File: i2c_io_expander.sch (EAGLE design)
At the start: 21 parts, among them IC1 MCP23017SP, J1 43814-6621, J6 22-23-2031

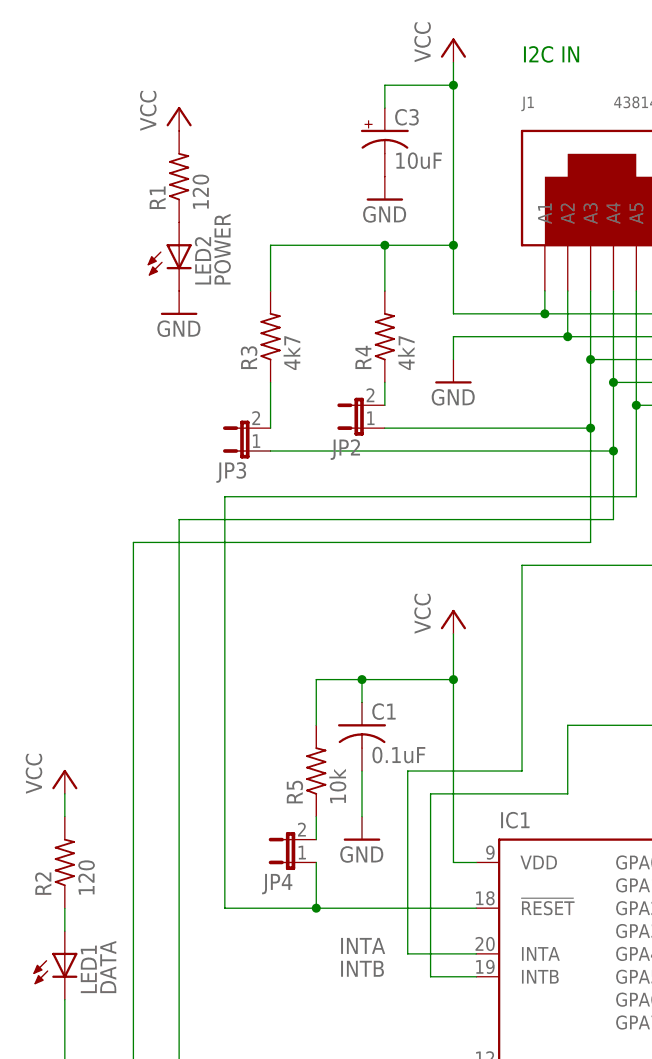
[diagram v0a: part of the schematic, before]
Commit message: Added contact info and rev # to silkscreen Added VCC and GND designator to silkscreen
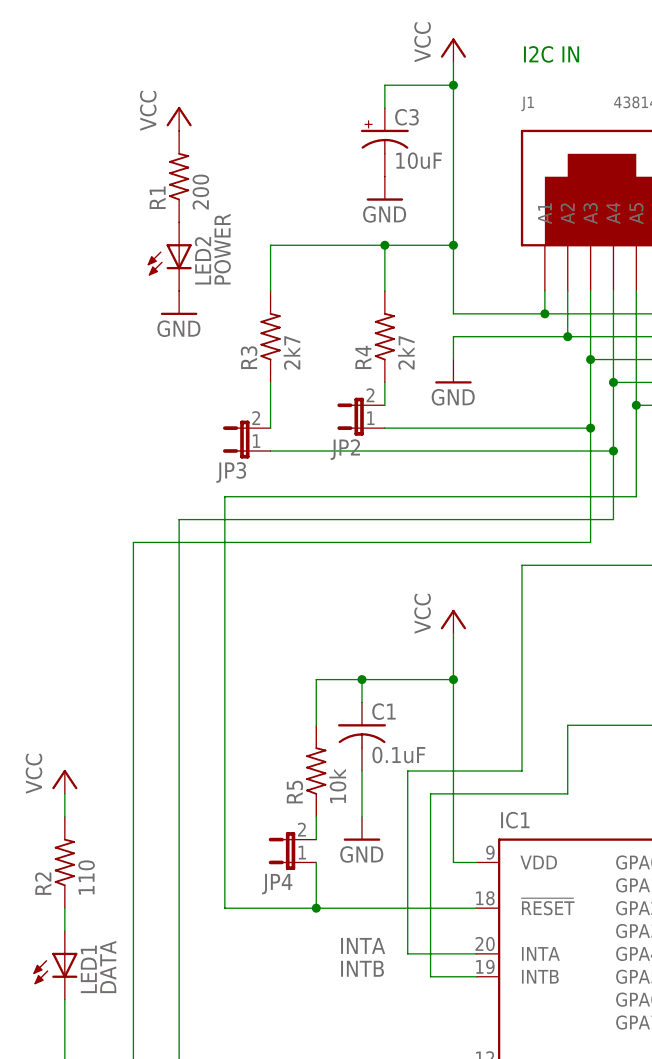
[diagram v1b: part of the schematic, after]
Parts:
- R1: value 120 -> 200
- R2: value 120 -> 110
- R3, R4: value 4k7 -> 2k7
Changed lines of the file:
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@@
 <attribute name="OC_NEWARK" value="unknown"/>
 </part>
-<part name="R1" library="rcl" deviceset="R-US_" device="R0603" value="120">
+<part name="R1" library="rcl" deviceset="R-US_" device="R0603" value="200">
 <attribute name="MF" value=""/>
 <attribute name="MPN" value=""/>
 <attribute name="OC_NEWARK" value="unknown"/>
 </part>
-<part name="R2" library="rcl" deviceset="R-US_" device="R0603" value="120">
+<part name="R2" library="rcl" deviceset="R-US_" device="R0603" value="110">
 <attribute name="MF" value=""/>
 <attribute name="MPN" value=""/>
 <attribute name="OC_NEWARK" value="unknown"/>
 </part>
-<part name="R3" library="rcl" deviceset="R-US_" device="R0603" value="4k7">
+<part name="R3" library="rcl" deviceset="R-US_" device="R0603" value="2k7">
 <attribute name="MF" value=""/>
 <attribute name="MPN" value=""/>
 <attribute name="OC_NEWARK" value="unknown"/>
 </part>
-<part name="R4" library="rcl" deviceset="R-US_" device="R0603" value="4k7">
+<part name="R4" library="rcl" deviceset="R-US_" device="R0603" value="2k7">
 <attribute name="MF" value=""/>
 <attribute name="MPN" value=""/>

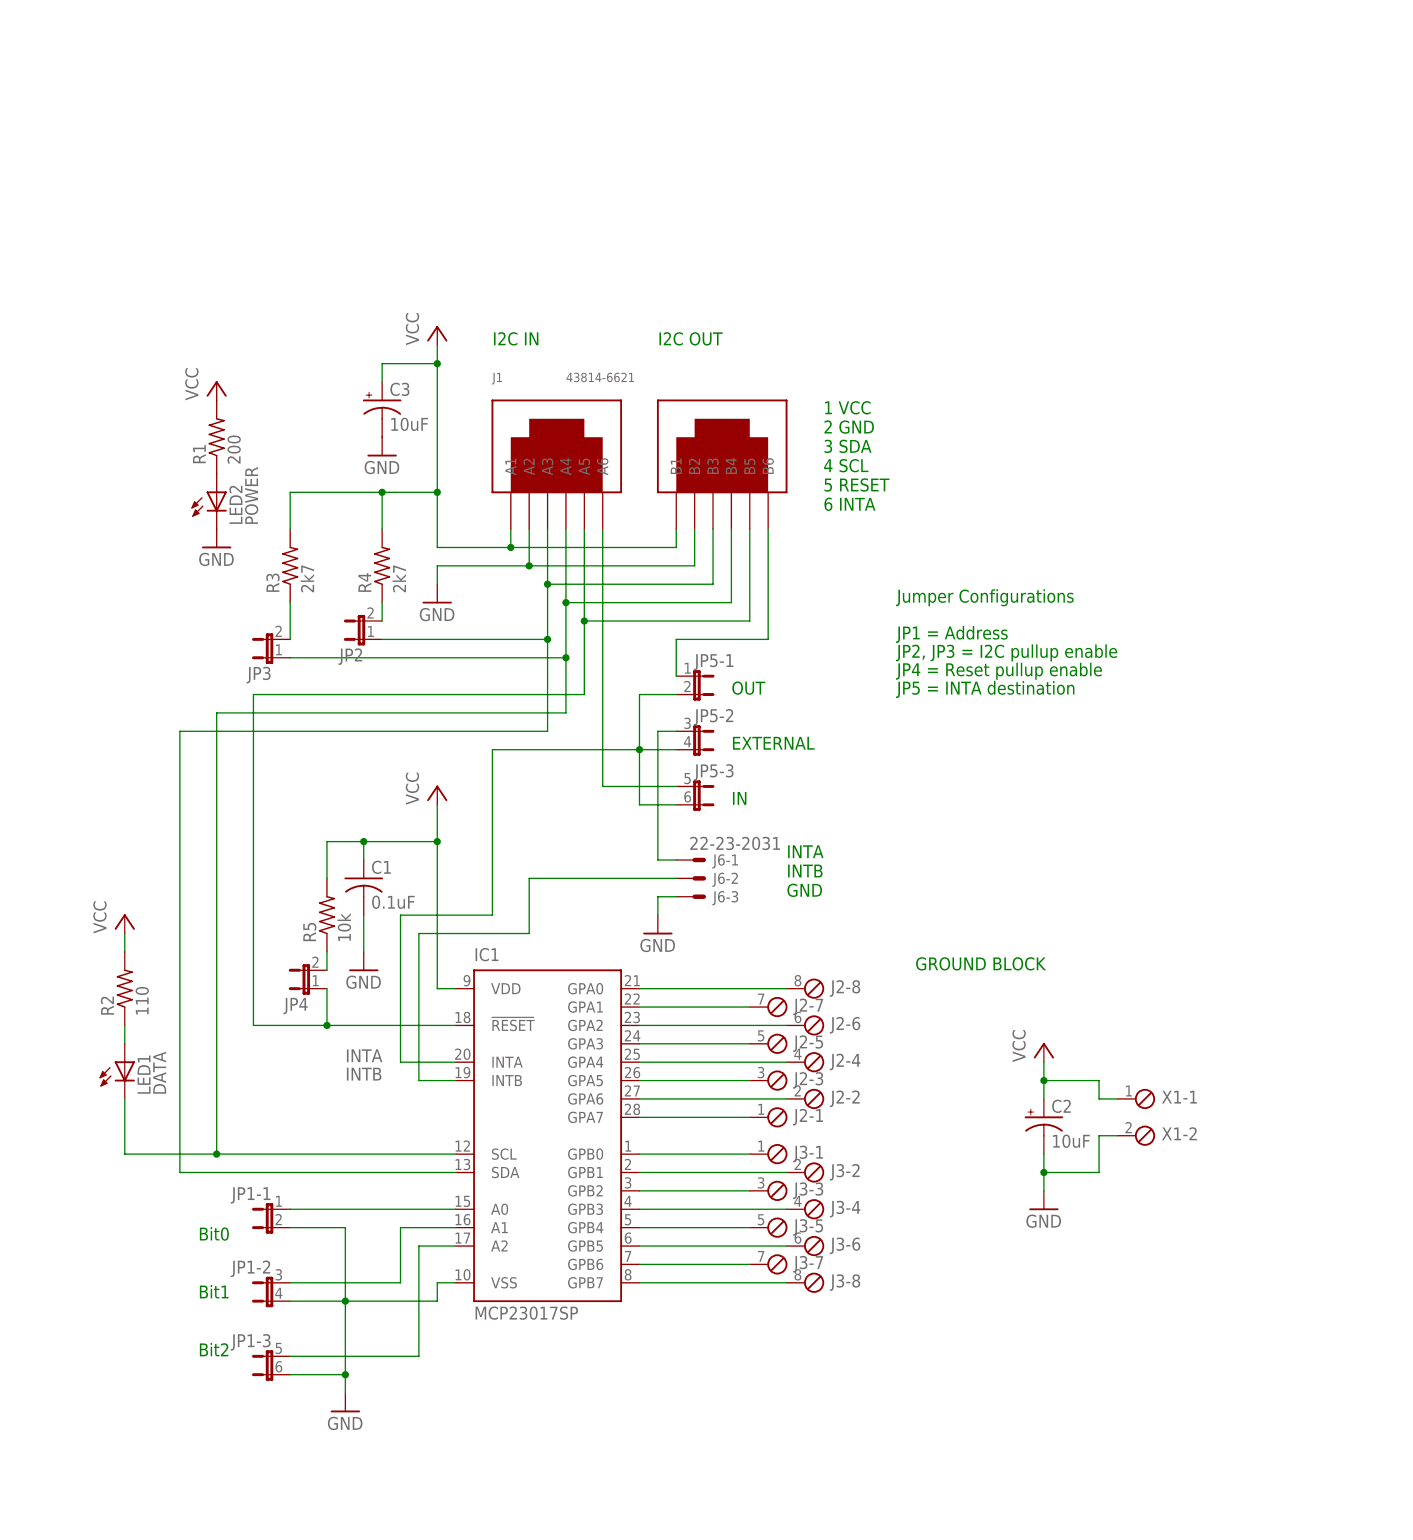
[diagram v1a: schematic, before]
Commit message: Added title block Added additional text to claify jumper settings
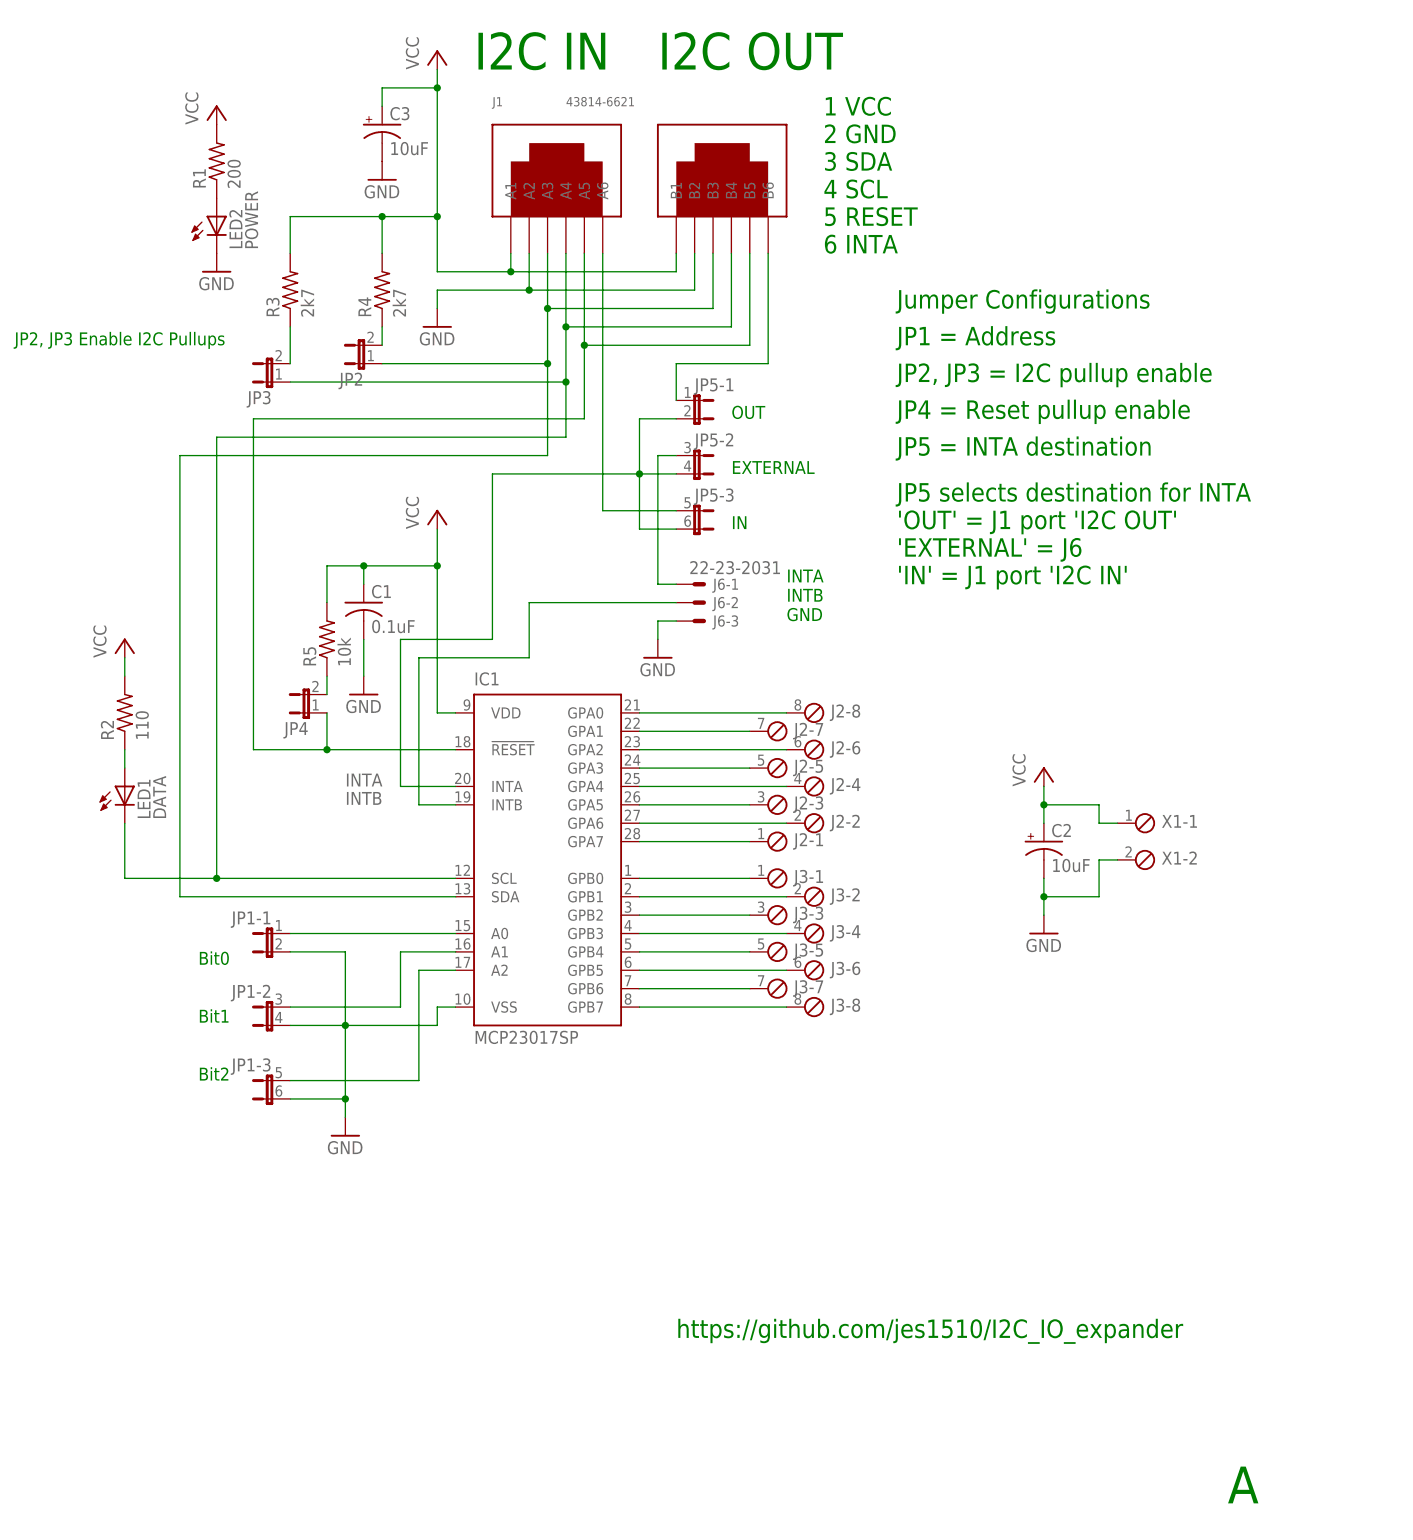
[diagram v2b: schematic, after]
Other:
- note added: "A"
- note added: "JP2, JP3 Enable I2C Pullups"
- note added: "JP5 selects destination for INTA 'OUT' = J1 port 'I2C OUT' 'EXTERNAL' = J6 'IN' = J1 port 'I2C IN'"
- note added: "https://github.com/jes1510/I2C_IO_expander"
- note removed: "GROUND BLOCK"
- moved on the sheet: C1, C2, C3, IC1, J1, J2-1, J2-2, J2-3, J2-4, J2-5, J2-6, J2-7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
